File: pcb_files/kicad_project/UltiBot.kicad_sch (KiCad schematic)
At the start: 0 parts

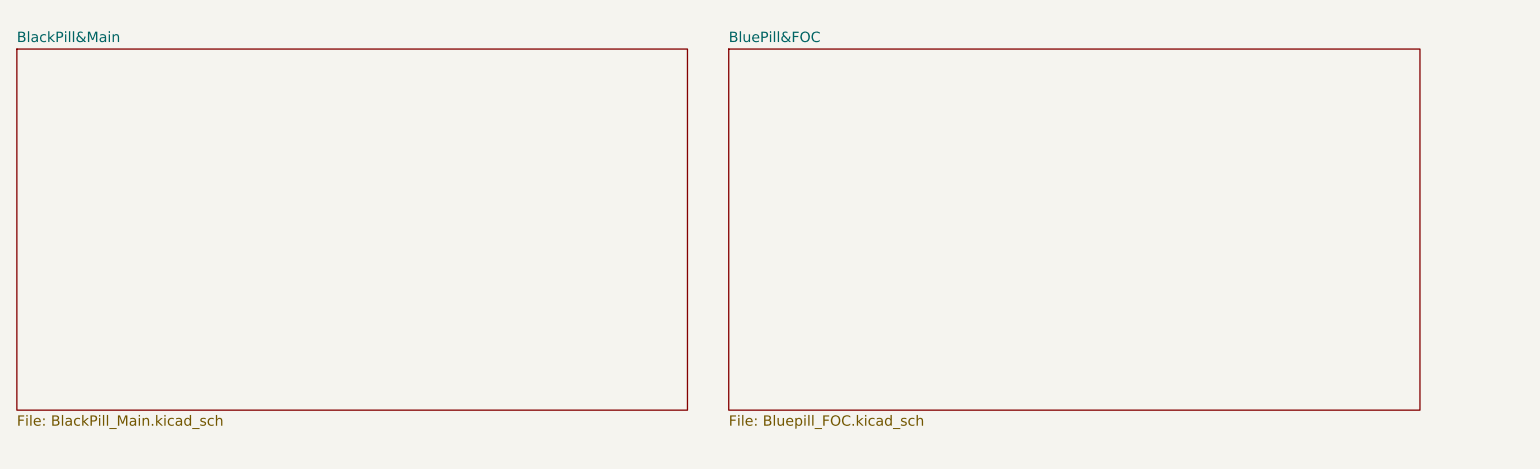
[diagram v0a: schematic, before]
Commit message: Añade pinout de BlackPill, completa esquemático y asocia footprints
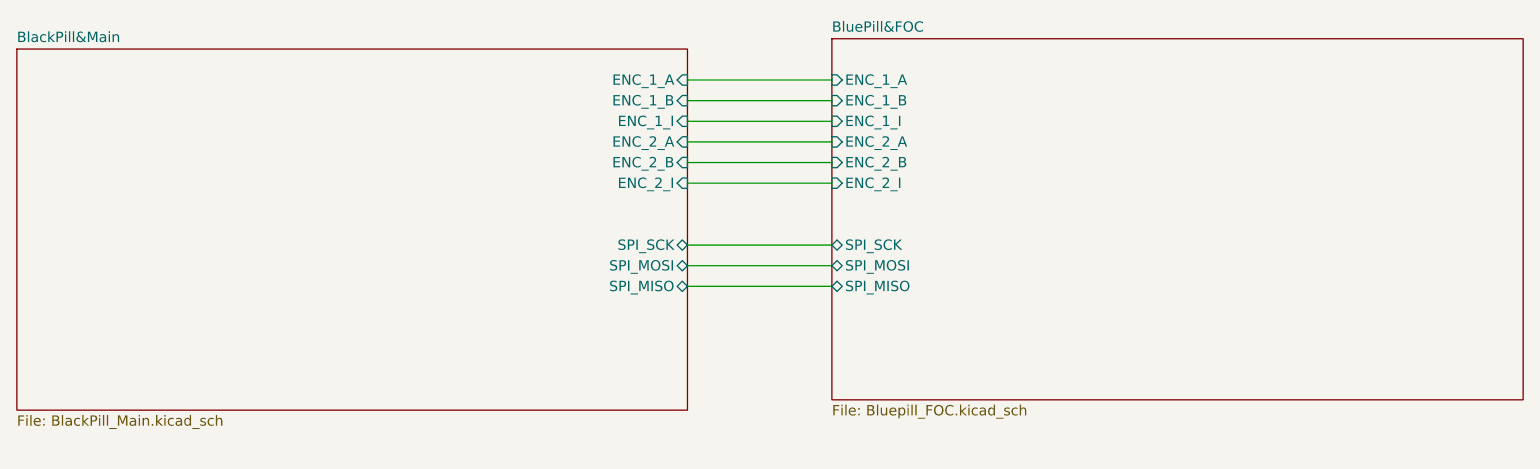
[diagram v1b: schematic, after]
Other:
- sheet BlackPill&Main ports: added ENC_1_A, ENC_1_B, ENC_1_I, ENC_2_A, ENC_2_B, ENC_2_I, SPI_MISO, SPI_MOSI, SPI_SCK; removed none
- sheet BluePill&FOC ports: added ENC_1_A, ENC_1_B, ENC_1_I, ENC_2_A, ENC_2_B, ENC_2_I, SPI_MISO, SPI_MOSI, SPI_SCK; removed none
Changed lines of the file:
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@@
 (kicad_sch (version 20230121) (generator eeschema)
   (paper "A4")
-  (sheet (at 111.76 22.86) (size 85.09 44.45) (fields_autoplaced)
+  (wire (pts (xy 106.68 49.53) (xy 124.46 49.53))
+    (stroke (width 0) (type default))
+  )
+  (wire (pts (xy 106.68 39.37) (xy 124.46 39.37))
+    (stroke (width 0) (type default))
+  )
+  (wire (pts (xy 106.68 29.21) (xy 124.46 29.21))
+    (stroke (width 0) (type default))
+  )
+  (wire (pts (xy 106.68 34.29) (xy 124.46 34.29))
+    (stroke (width 0) (type default))
+  )
+  (wire (pts (xy 106.68 36.83) (xy 124.46 36.83))
+    (stroke (width 0) (type default))
+  )
+  (wire (pts (xy 106.68 52.07) (xy 124.46 52.07))
+    (stroke (width 0) (type default))
+  )
+  (wire (pts (xy 106.68 26.67) (xy 124.46 26.67))
+    (stroke (width 0) (type default))
+  )
+  (wire (pts (xy 106.68 31.75) (xy 124.46 31.75))
+    (stroke (width 0) (type default))
+  )
+  (wire (pts (xy 106.68 46.99) (xy 124.46 46.99))
+    (stroke (width 0) (type default))
+  )
+  (sheet (at 124.46 21.59) (size 85.09 44.45) (fields_autoplaced)
     (stroke (width 0.1524) (type solid))
     (fill (color 0 0 0 0.0000))
-    (property "Sheetname" "BluePill&FOC" (at 111.76 22.1484 0)
+    (property "Sheetname" "BluePill&FOC" (at 124.46 20.8784 0)
       (effects (font (size 1.27 1.27)) (justify left bottom))
     )
-    (property "Sheetfile" "Bluepill_FOC.kicad_sch" (at 111.76 67.8946 0)
+    (property "Sheetfile" "Bluepill_FOC.kicad_sch" (at 124.46 66.6246 0)
       (effects (font (size 1.27 1.27)) (justify left top))
+    )
+    (pin "SPI_SCK" bidirectional (at 124.46 46.99 180)
+      (effects (font (size 1.27 1.27)) (justify left))
+    )
+    (pin "SPI_MOSI" bidirectional (at 124.46 49.53 180)
+      (effects (font (size 1.27 1.27)) (justify left))
+    )
+    (pin "SPI_MISO" bidirectional (at 124.46 52.07 180)
+      (effects (font (size 1.27 1.27)) (justify left))
+    )
+    (pin "ENC_1_B" input (at 124.46 29.21 180)
+      (effects (font (size 1.27 1.27)) (justify left))
+    )
+    (pin "ENC_1_I" input (at 124.46 31.75 180)
+      (effects (font (size 1.27 1.27)) (justify left))
+    )
+    (pin "ENC_2_I" input (at 124.46 39.37 180)
+      (effects (font (size 1.27 1.27)) (justify left))
+    )
+    (pin "ENC_2_B" input (at 124.46 36.83 180)
+      (effects (font (size 1.27 1.27)) (justify left))
+    )
+    (pin "ENC_2_A" input (at 124.46 34.29 180)
+      (effects (font (size 1.27 1.27)) (justify left))
+    )
+    (pin "ENC_1_A" input (at 124.46 26.67 180)
+      (effects (font (size 1.27 1.27)) (justify left))
     )
     (instances
@@
       (effects (font (size 1.27 1.27)) (justify left top))
     )
+    (pin "ENC_2_I" input (at 106.68 39.37 0)
+      (effects (font (size 1.27 1.27)) (justify right))
+    )
+    (pin "ENC_2_B" input (at 106.68 36.83 0)
+      (effects (font (size 1.27 1.27)) (justify right))
+    )
+    (pin "ENC_1_I" input (at 106.68 31.75 0)
+      (effects (font (size 1.27 1.27)) (justify right))
+    )
+    (pin "ENC_1_B" input (at 106.68 29.21 0)
+      (effects (font (size 1.27 1.27)) (justify right))
+    )
+    (pin "ENC_1_A" input (at 106.68 26.67 0)
+      (effects (font (size 1.27 1.27)) (justify right))
+    )
+    (pin "ENC_2_A" input (at 106.68 34.29 0)
+      (effects (font (size 1.27 1.27)) (justify right))
+    )
+    (pin "SPI_SCK" bidirectional (at 106.68 46.99 0)
+      (effects (font (size 1.27 1.27)) (justify right))
+    )
+    (pin "SPI_MISO" bidirectional (at 106.68 52.07 0)
+      (effects (font (size 1.27 1.27)) (justify right))
+    )
+    (pin "SPI_MOSI" bidirectional (at 106.68 49.53 0)
+      (effects (font (size 1.27 1.27)) (justify right))
+    )
     (instances

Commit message: Actualiza el esquemático de la PCB
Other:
- sheet BlackPill&Main ports: added SPI_NSS, USART6_RX, USART6_TX; removed none
- sheet BluePill&FOC ports: added SPI_NSS, USART3_RX, USART3_TX; removed none
- note added: "X"
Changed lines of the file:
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@@
+    (stroke (width 0) (type default))
+  )
+  (wire (pts (xy 106.68 54.61) (xy 124.46 54.61))
     (stroke (width 0) (type default))
   )
@@
     (stroke (width 0) (type default))
   )
+  (wire (pts (xy 106.68 62.23) (xy 124.46 62.23))
+    (stroke (width 0) (type default))
+  )
   (wire (pts (xy 106.68 26.67) (xy 124.46 26.67))
     (stroke (width 0) (type default))
@@
     (stroke (width 0) (type default))
   )
+  (wire (pts (xy 106.68 59.69) (xy 124.46 59.69))
+    (stroke (width 0) (type default))
+  )
   (wire (pts (xy 106.68 46.99) (xy 124.46 46.99))
     (stroke (width 0) (type default))
+  )
+  (text "X" (at 114.808 61.976 0)
+    (effects (font (size 1.27 1.27)) (justify left bottom))
   )
   (sheet (at 124.46 21.59) (size 85.09 44.45) (fields_autoplaced)
@@
     )
     (pin "ENC_1_A" input (at 124.46 26.67 180)
+      (effects (font (size 1.27 1.27)) (justify left))
+    )
+    (pin "SPI_NSS" bidirectional (at 124.46 54.61 180)
+      (effects (font (size 1.27 1.27)) (justify left))
+    )
+    (pin "USART3_RX" input (at 124.46 59.69 180)
+      (effects (font (size 1.27 1.27)) (justify left))
+    )
+    (pin "USART3_TX" input (at 124.46 62.23 180)
       (effects (font (size 1.27 1.27)) (justify left))
     )
@@
       (effects (font (size 1.27 1.27)) (justify right))
     )
+    (pin "SPI_NSS" bidirectional (at 106.68 54.61 0)
+      (effects (font (size 1.27 1.27)) (justify right))
+    )
+    (pin "USART6_TX" input (at 106.68 59.69 0)
+      (effects (font (size 1.27 1.27)) (justify right))
+    )
+    (pin "USART6_RX" input (at 106.68 62.23 0)
+      (effects (font (size 1.27 1.27)) (justify right))
+    )

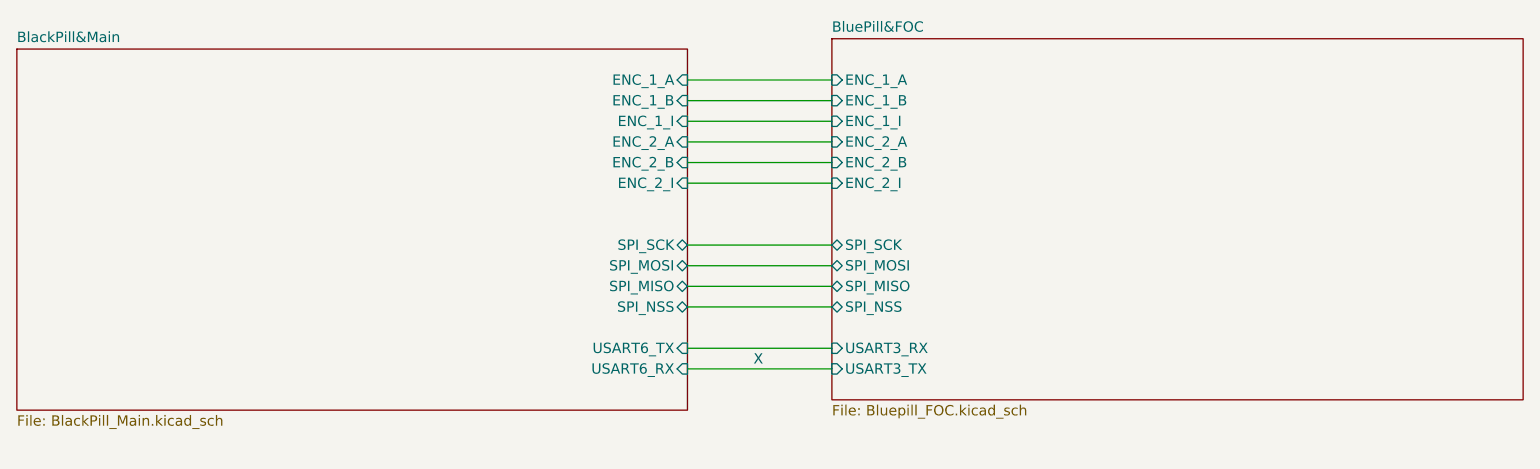
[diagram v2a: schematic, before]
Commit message: Actualiza esquemático y finaliza ruteado de PCB
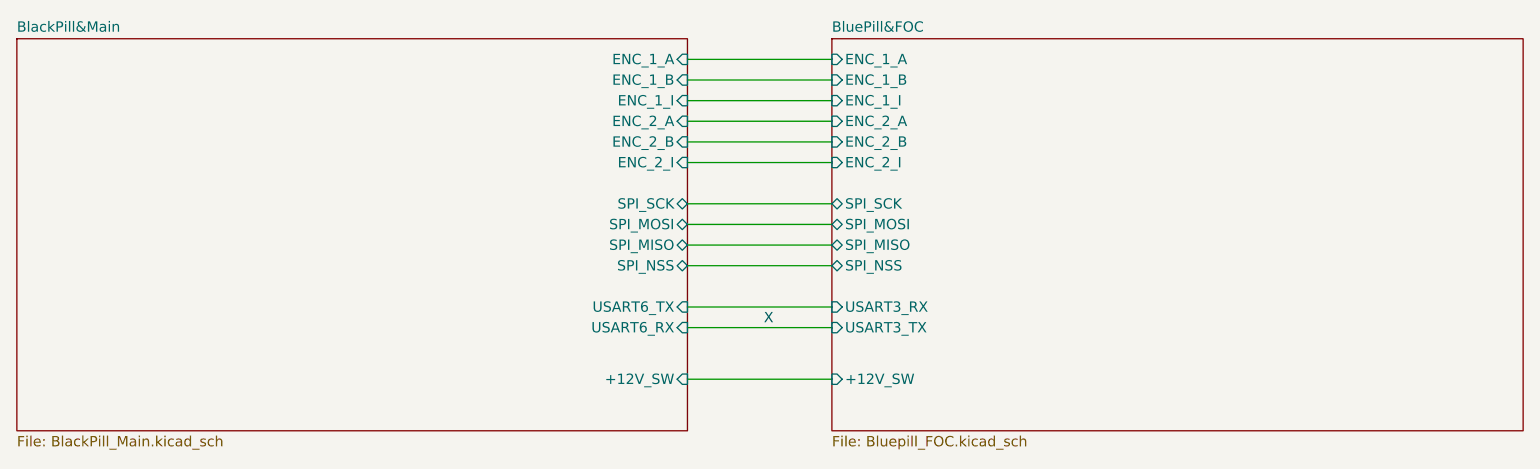
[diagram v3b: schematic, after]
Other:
- sheet BlackPill&Main ports: added +12V_SW; removed none
- sheet BluePill&FOC ports: added +12V_SW; removed none
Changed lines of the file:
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@@
 (kicad_sch (version 20230121) (generator eeschema)
   (paper "A4")
-  (wire (pts (xy 106.68 49.53) (xy 124.46 49.53))
-    (stroke (width 0) (type default))
-  )
-  (wire (pts (xy 106.68 39.37) (xy 124.46 39.37))
-    (stroke (width 0) (type default))
-  )
-  (wire (pts (xy 106.68 54.61) (xy 124.46 54.61))
-    (stroke (width 0) (type default))
-  )
-  (wire (pts (xy 106.68 29.21) (xy 124.46 29.21))
-    (stroke (width 0) (type default))
-  )
-  (wire (pts (xy 106.68 34.29) (xy 124.46 34.29))
+  (wire (pts (xy 106.68 44.45) (xy 124.46 44.45))
     (stroke (width 0) (type default))
   )
@@
     (stroke (width 0) (type default))
   )
-  (wire (pts (xy 106.68 52.07) (xy 124.46 52.07))
-    (stroke (width 0) (type default))
-  )
-  (wire (pts (xy 106.68 62.23) (xy 124.46 62.23))
+  (wire (pts (xy 106.68 49.53) (xy 124.46 49.53))
     (stroke (width 0) (type default))
   )
@@
     (stroke (width 0) (type default))
   )
-  (wire (pts (xy 106.68 59.69) (xy 124.46 59.69))
+  (wire (pts (xy 106.68 34.29) (xy 124.46 34.29))
+    (stroke (width 0) (type default))
+  )
+  (wire (pts (xy 106.68 63.5) (xy 124.46 63.5))
     (stroke (width 0) (type default))
   )
@@
     (stroke (width 0) (type default))
   )
-  (text "X" (at 114.808 61.976 0)
+  (wire (pts (xy 106.68 57.15) (xy 124.46 57.15))
+    (stroke (width 0) (type default))
+  )
+  (wire (pts (xy 106.68 24.13) (xy 124.46 24.13))
+    (stroke (width 0) (type default))
+  )
+  (wire (pts (xy 106.68 29.21) (xy 124.46 29.21))
+    (stroke (width 0) (type default))
+  )
+  (wire (pts (xy 106.68 54.61) (xy 124.46 54.61))
+    (stroke (width 0) (type default))
+  )
+  (wire (pts (xy 106.68 41.91) (xy 124.46 41.91))
+    (stroke (width 0) (type default))
+  )
+  (text "X" (at 116.078 56.896 0)
     (effects (font (size 1.27 1.27)) (justify left bottom))
   )
-  (sheet (at 124.46 21.59) (size 85.09 44.45) (fields_autoplaced)
+  (sheet (at 124.46 21.59) (size 85.09 48.26) (fields_autoplaced)
     (stroke (width 0.1524) (type solid))
     (fill (color 0 0 0 0.0000))
@@
       (effects (font (size 1.27 1.27)) (justify left bottom))
     )
-    (property "Sheetfile" "Bluepill_FOC.kicad_sch" (at 124.46 66.6246 0)
+    (property "Sheetfile" "Bluepill_FOC.kicad_sch" (at 124.46 70.4346 0)
       (effects (font (size 1.27 1.27)) (justify left top))
     )
-    (pin "SPI_SCK" bidirectional (at 124.46 46.99 180)
+    (pin "SPI_SCK" bidirectional (at 124.46 41.91 180)
       (effects (font (size 1.27 1.27)) (justify left))
     )
-    (pin "SPI_MOSI" bidirectional (at 124.46 49.53 180)
+    (pin "SPI_MOSI" bidirectional (at 124.46 44.45 180)
       (effects (font (size 1.27 1.27)) (justify left))
     )
-    (pin "SPI_MISO" bidirectional (at 124.46 52.07 180)
+    (pin "SPI_MISO" bidirectional (at 124.46 46.99 180)
       (effects (font (size 1.27 1.27)) (justify left))
     )
-    (pin "ENC_1_B" input (at 124.46 29.21 180)
+    (pin "ENC_1_B" input (at 124.46 26.67 180)
       (effects (font (size 1.27 1.27)) (justify left))
     )
-    (pin "ENC_1_I" input (at 124.46 31.75 180)
+    (pin "ENC_1_I" input (at 124.46 29.21 180)
       (effects (font (size 1.27 1.27)) (justify left))
     )
-    (pin "ENC_2_I" input (at 124.46 39.37 180)
+    (pin "ENC_2_I" input (at 124.46 36.83 180)
       (effects (font (size 1.27 1.27)) (justify left))
     )
-    (pin "ENC_2_B" input (at 124.46 36.83 180)
+    (pin "ENC_2_B" input (at 124.46 34.29 180)
       (effects (font (size 1.27 1.27)) (justify left))
     )
-    (pin "ENC_2_A" input (at 124.46 34.29 180)
+    (pin "ENC_2_A" input (at 124.46 31.75 180)
       (effects (font (size 1.27 1.27)) (justify left))
     )
-    (pin "ENC_1_A" input (at 124.46 26.67 180)
+    (pin "ENC_1_A" input (at 124.46 24.13 180)
       (effects (font (size 1.27 1.27)) (justify left))
     )
-    (pin "SPI_NSS" bidirectional (at 124.46 54.61 180)
+    (pin "SPI_NSS" bidirectional (at 124.46 49.53 180)
       (effects (font (size 1.27 1.27)) (justify left))
     )
-    (pin "USART3_RX" input (at 124.46 59.69 180)
+    (pin "USART3_RX" input (at 124.46 54.61 180)
       (effects (font (size 1.27 1.27)) (justify left))
     )
-    (pin "USART3_TX" input (at 124.46 62.23 180)
+    (pin "USART3_TX" input (at 124.46 57.15 180)
+      (effects (font (size 1.27 1.27)) (justify left))
+    )
+    (pin "+12V_SW" input (at 124.46 63.5 180)
       (effects (font (size 1.27 1.27)) (justify left))
     )
@@
     )
   )
-  (sheet (at 24.13 22.86) (size 82.55 44.45) (fields_autoplaced)
+  (sheet (at 24.13 21.59) (size 82.55 48.26) (fields_autoplaced)
     (stroke (width 0.1524) (type solid))
     (fill (color 0 0 0 0.0000))
-    (property "Sheetname" "BlackPill&Main" (at 24.13 22.1484 0)
+    (property "Sheetname" "BlackPill&Main" (at 24.13 20.8784 0)
       (effects (font (size 1.27 1.27)) (justify left bottom))
     )
-    (property "Sheetfile" "BlackPill_Main.kicad_sch" (at 24.13 67.8946 0)
+    (property "Sheetfile" "BlackPill_Main.kicad_sch" (at 24.13 70.4346 0)
       (effects (font (size 1.27 1.27)) (justify left top))
     )
-    (pin "ENC_2_I" input (at 106.68 39.37 0)
+    (pin "ENC_2_I" input (at 106.68 36.83 0)
       (effects (font (size 1.27 1.27)) (justify right))
     )
-    (pin "ENC_2_B" input (at 106.68 36.83 0)
+    (pin "ENC_2_B" input (at 106.68 34.29 0)
       (effects (font (size 1.27 1.27)) (justify right))
     )
-    (pin "ENC_1_I" input (at 106.68 31.75 0)
+    (pin "ENC_1_I" input (at 106.68 29.21 0)
       (effects (font (size 1.27 1.27)) (justify right))
     )
-    (pin "ENC_1_B" input (at 106.68 29.21 0)
+    (pin "ENC_1_B" input (at 106.68 26.67 0)
       (effects (font (size 1.27 1.27)) (justify right))
     )
-    (pin "ENC_1_A" input (at 106.68 26.67 0)
+    (pin "ENC_1_A" input (at 106.68 24.13 0)
       (effects (font (size 1.27 1.27)) (justify right))
     )
-    (pin "ENC_2_A" input (at 106.68 34.29 0)
+    (pin "ENC_2_A" input (at 106.68 31.75 0)
       (effects (font (size 1.27 1.27)) (justify right))
     )
-    (pin "SPI_SCK" bidirectional (at 106.68 46.99 0)
+    (pin "SPI_SCK" bidirectional (at 106.68 41.91 0)
       (effects (font (size 1.27 1.27)) (justify right))
     )
-    (pin "SPI_MISO" bidirectional (at 106.68 52.07 0)
+    (pin "SPI_MISO" bidirectional (at 106.68 46.99 0)
       (effects (font (size 1.27 1.27)) (justify right))
     )
-    (pin "SPI_MOSI" bidirectional (at 106.68 49.53 0)
+    (pin "SPI_MOSI" bidirectional (at 106.68 44.45 0)
       (effects (font (size 1.27 1.27)) (justify right))
     )
-    (pin "SPI_NSS" bidirectional (at 106.68 54.61 0)
+    (pin "SPI_NSS" bidirectional (at 106.68 49.53 0)
       (effects (font (size 1.27 1.27)) (justify right))
     )
-    (pin "USART6_TX" input (at 106.68 59.69 0)
+    (pin "USART6_TX" input (at 106.68 54.61 0)
       (effects (font (size 1.27 1.27)) (justify right))
     )
-    (pin "USART6_RX" input (at 106.68 62.23 0)
+    (pin "USART6_RX" input (at 106.68 57.15 0)
       (effects (font (size 1.27 1.27)) (justify right))
     )
+    (pin "+12V_SW" input (at 106.68 63.5 0)
+      (effects (font (size 1.27 1.27)) (justify right))
+    )
